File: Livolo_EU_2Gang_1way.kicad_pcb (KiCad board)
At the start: 2 copper layers, 43 x 43 mm, 51 parts, among them IC1 ATMEGA328P, U1 ATSHA204A, U2 RFM69CW, U3 MIC5205-3.3, U4 MCP16301

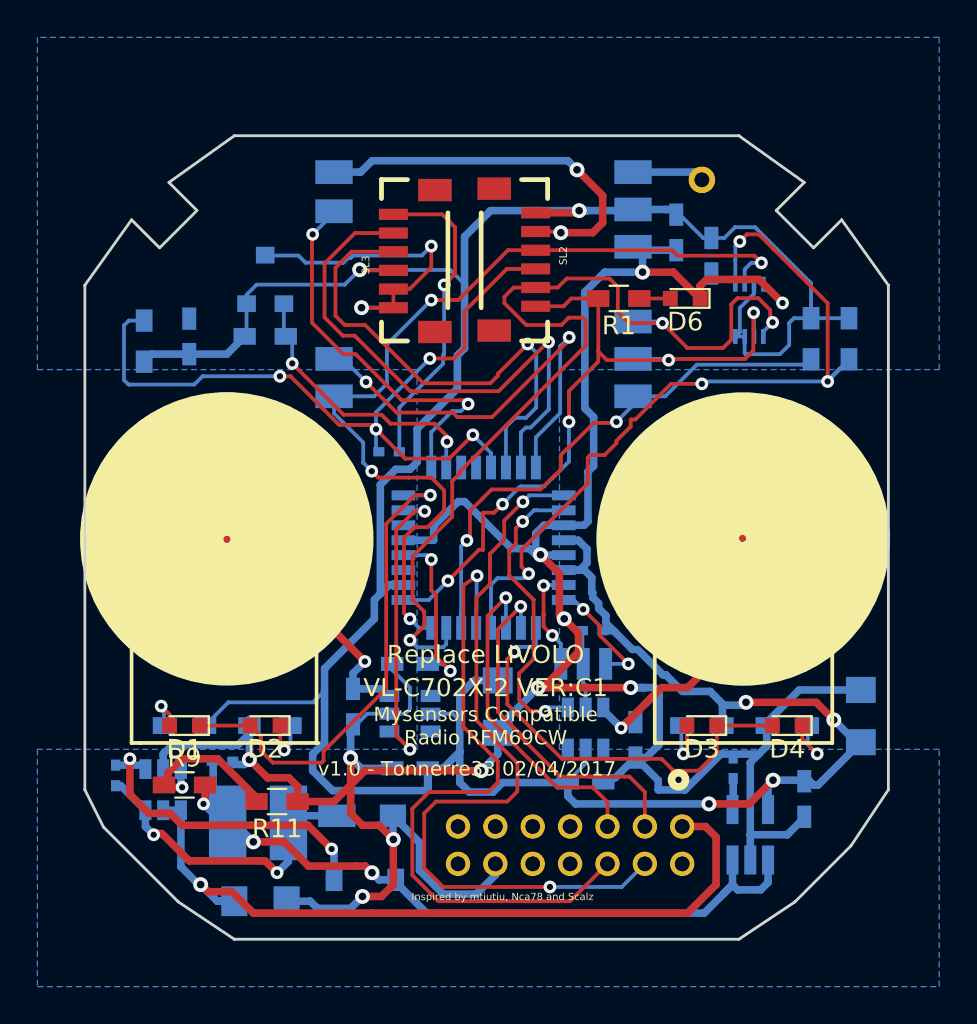
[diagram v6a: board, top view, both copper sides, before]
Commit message: replace bad footprint AT25DF512C
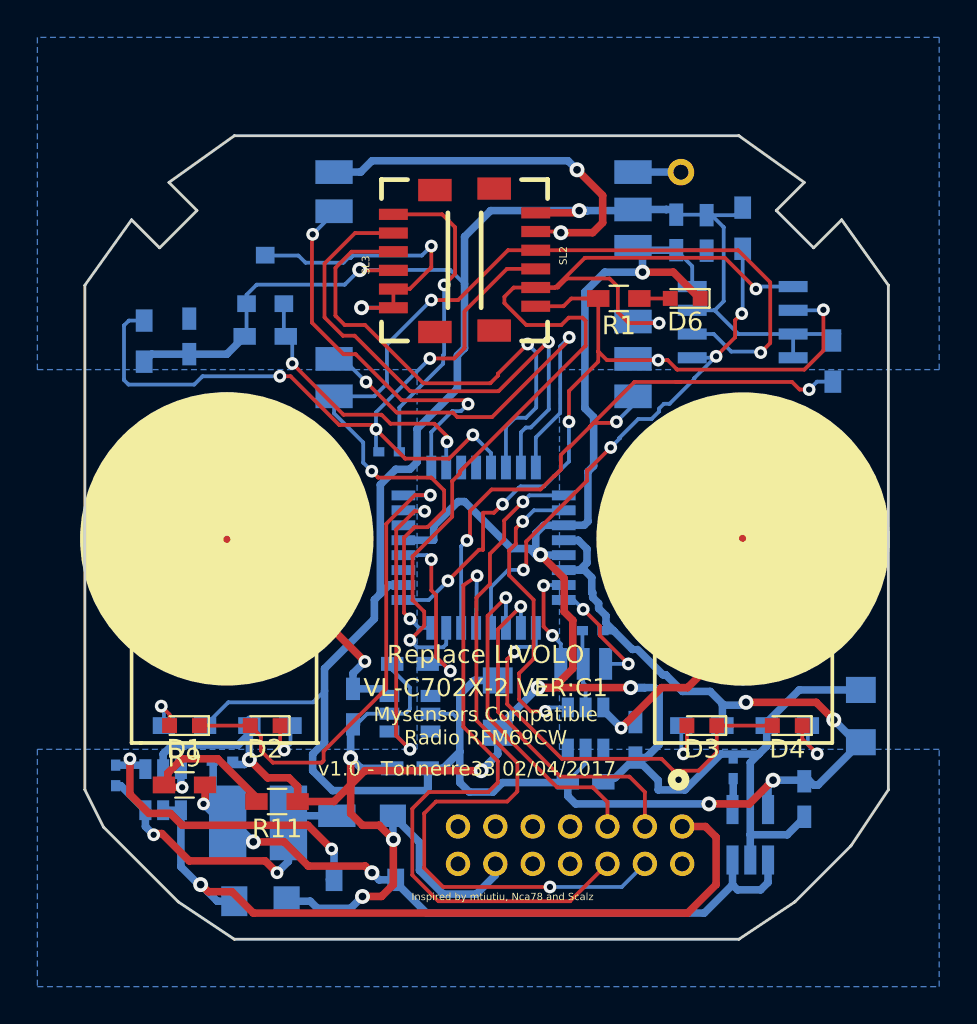
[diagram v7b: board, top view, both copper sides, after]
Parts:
- removed U$8: AT25DF512C_MAHNT, Livolo_EU_2Gang_1way:AT25DF512C_MAHNT
- added U5: AT25DF512C, SOIC-8_3.9x4.9mm_Pitch1.27mm, B.Cu at (162.2, 93.5)
- moved R10 8.21 mm to (162.2, 88.5)
- moved R4 1.67 mm to (167.0, 95.6)
- moved C14 1.25 mm to (160.3, 88.7)
- moved U$7 1.19 mm to (158.9, 85.5)
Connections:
- net /3VCC_1 renamed /3.3VCC_1
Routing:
- net /FLASH_CS: track 43.7 -> 28.4 mm
- net /MISO: track 48.3 -> 55.3 mm
- net VCC: track 178.3 -> 173.6 mm
- net /MOSI: track 52.7 -> 57.0 mm
- net /SCK: track 39.9 -> 44.0 mm
- net GND: track 204.2 -> 200.8 mm, vias 15 -> 13
- net /CSN: track 29.8 -> 33.1 mm, vias 2 -> 3
- net Net-(U$7-PadP$1): track 3.86 -> 2.57 mm
- net /+12VCC: track 41.9 -> 41.0 mm
- net /3.3VCC_1: track 41.0 -> 40.3 mm
- net Net-(C4-Pad2): track 20.8 -> 20.3 mm

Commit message: cleaning
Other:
- board text added: "v1.0 - Tonnerre33 08/04/2017"
- board text removed: "v1.0 - Tonnerre33 02/04/2017"
